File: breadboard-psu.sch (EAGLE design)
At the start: 23 parts, among them J1 DC_IN, J2 5V-BOARD, J3 5V-CABLE, J4 3.3V-BOARD, J5 3.3V-CABLE, K1 POWER, K2 5V, K3 3.3V, U1 AP1117T50G-U, U2 AP1117T33G-U

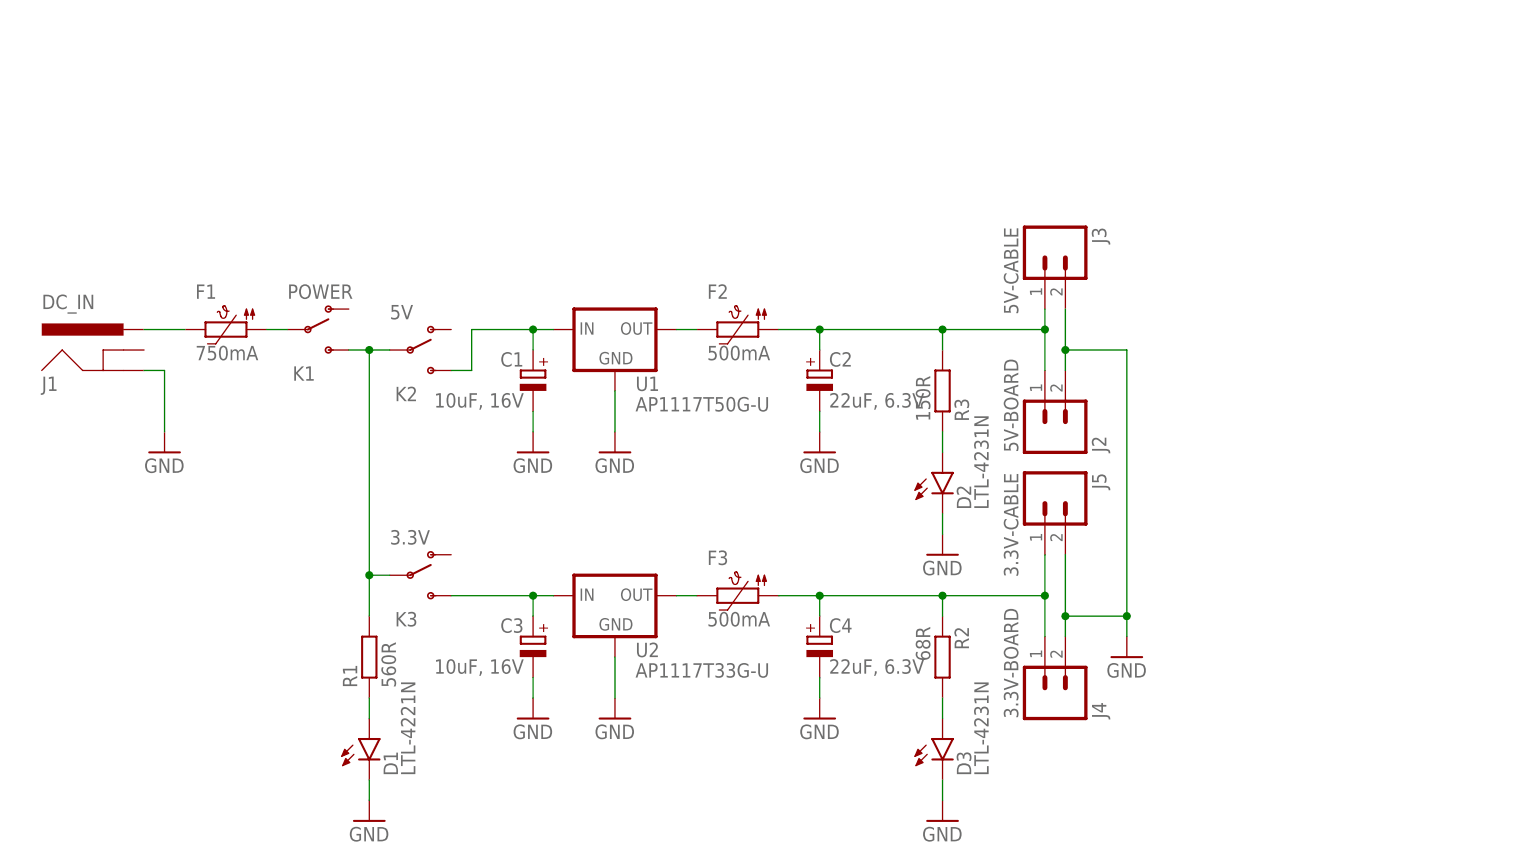
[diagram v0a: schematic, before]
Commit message: UPDATE:  - first draft, schematic is stable, layout is routed and poured.  - still left to do the silkscreen and confirm width (to match breadboard).  - all footprints checked or generated in-situ to match the actual BOM.
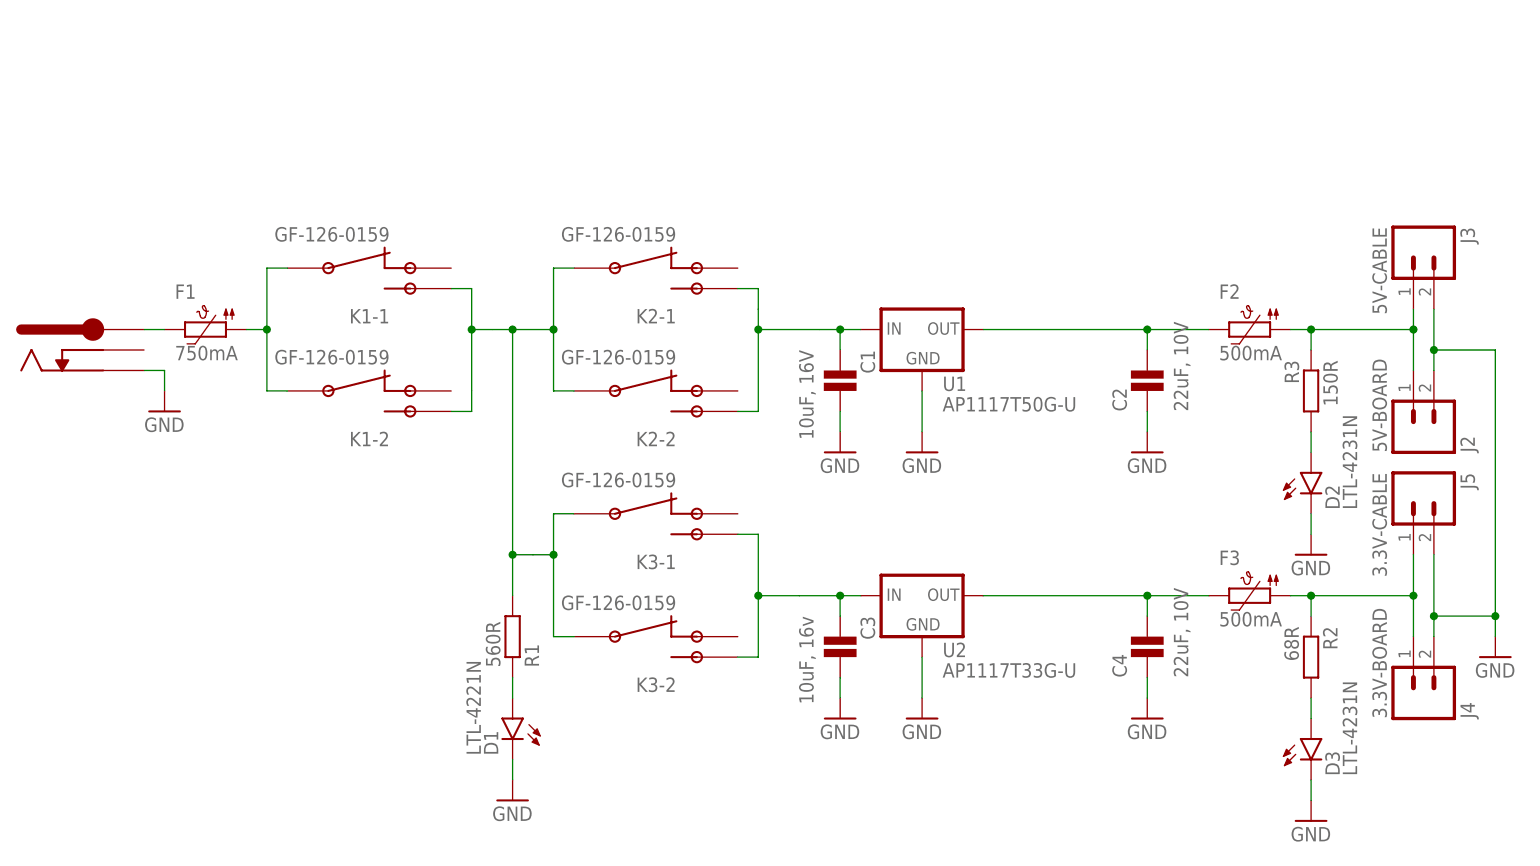
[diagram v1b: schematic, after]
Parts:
- C1: device rcl:CPOL-EUETR3 -> radu-collected:FK26X7R
- C2, C4: value 22uF, 6.3V -> 22uF, 10V; device rcl:CPOL-EUETR3 -> radu-collected:FK20X7R
- C3: value 10uF, 16V -> 10uF, 16v; device rcl:CPOL-EUETR3 -> radu-collected:FK26X7R
- J1: value DC_IN -> 163-5010-E; device SparkFun-Connectors:POWER_JACKSLT -> radu-collected:163-5010-E
- K1: value POWER -> GF-126-0159; device SparkFun-Electromechanical:SWITCH-SPDTPTH -> radu-collected:GF-126-0159
- K2: value 5V -> GF-126-0159; device SparkFun-Electromechanical:SWITCH-SPDTPTH -> radu-collected:GF-126-0159
- K3: value 3.3V -> GF-126-0159; device SparkFun-Electromechanical:SWITCH-SPDTPTH -> radu-collected:GF-126-0159
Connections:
- net 3V3: no longer C4.+
- net 5V: now also R3.1; no longer C2.+, R3.2
- net GND: now also C1.P$2, C2.P$1, C3.P$2, C4.P$1, J1.-; no longer C1.-, C2.-, C3.-, C4.-, J1.GND
- net N$1: now also J1.+; no longer J1.PWR
- net N$10: now also R3.2; no longer R3.1
- net N$2: now also K1-1.P$1, K1-2.P$1; no longer K1.P
- net N$3: now also K1-1.P$3, K1-2.P$3, K2-1.P$1, K2-2.P$1, K3-1.P$1, K3-2.P$1; no longer K1.S, K2.P, K3.P
- net N$4: now also C1.P$1, K2-1.P$3, K2-2.P$3; no longer C1.+, K2.S
- net N$5: now also C3.P$1, K3-1.P$3, K3-2.P$3; no longer C3.+, K3.S
- net N$6: now also C2.P$2
- net N$7: now also C4.P$2
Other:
- moved on the sheet: D1, D2, D3, F1, F2, F3, J2, J3, J4, J5, R1, R2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

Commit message: UPDATE:  - redesigned without fangs as various breadboards have various widths, leaving just cable version in  - this allows us to fit in 5x5cm with drastic reduction in price
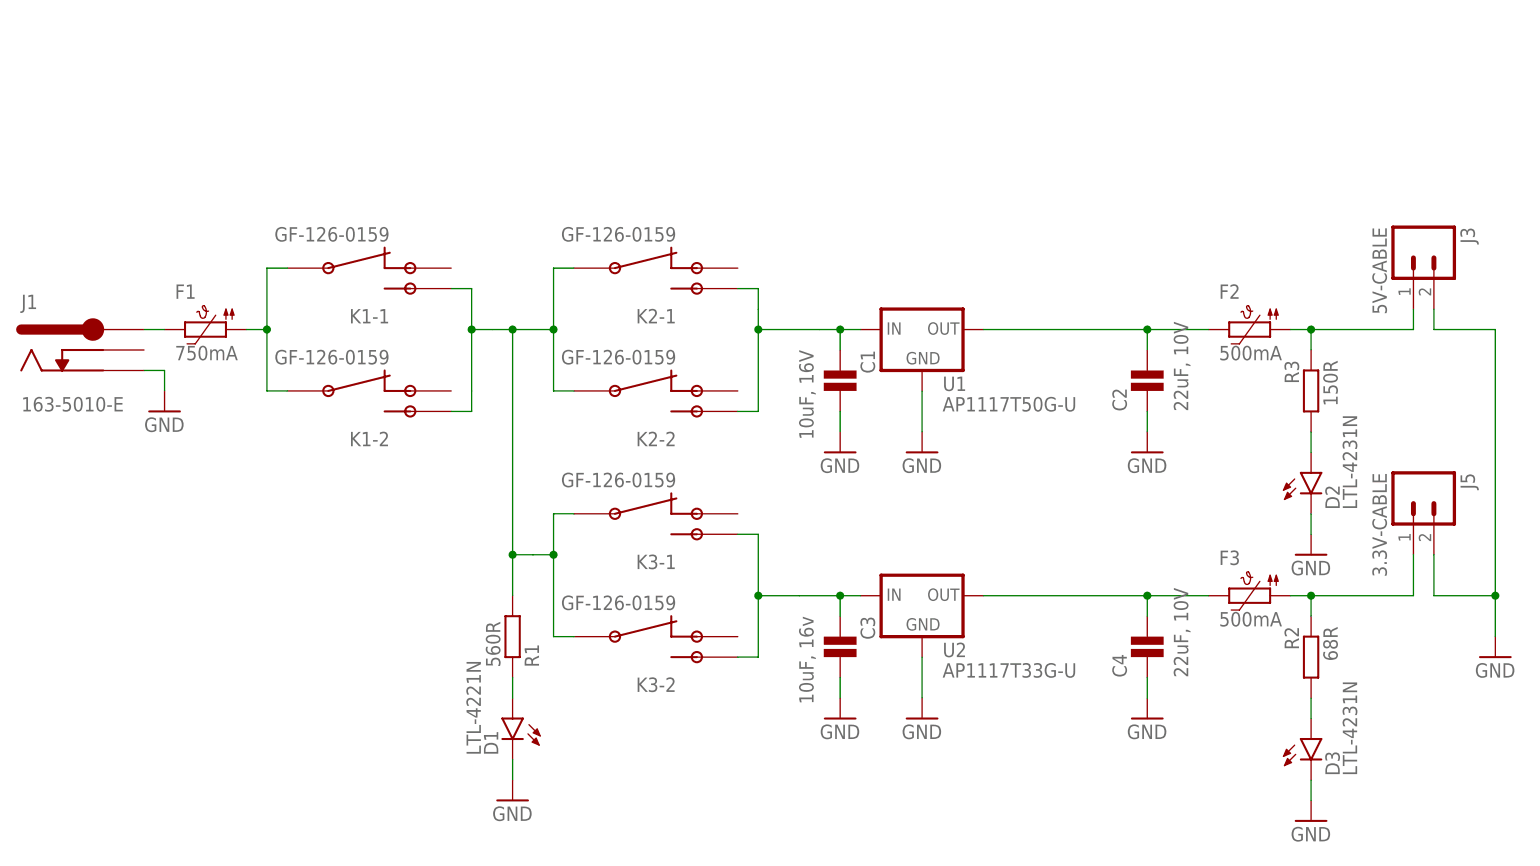
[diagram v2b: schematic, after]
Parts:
- removed J2: 5V-BOARD, SparkFun-Connectors:M02PTH
- removed J4: 3.3V-BOARD, SparkFun-Connectors:M02PTH
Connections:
- net 3V3: no longer J4.1
- net 5V: no longer J2.1
- net GND: no longer J2.2, J4.2
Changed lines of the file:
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@@
 <part name="GND2" library="SparkFun-Aesthetics" deviceset="GND" device=""/>
 <part name="GND3" library="SparkFun-Aesthetics" deviceset="GND" device=""/>
-<part name="J4" library="SparkFun-Connectors" deviceset="M02" device="PTH" value="3.3V-BOARD"/>
-<part name="J2" library="SparkFun-Connectors" deviceset="M02" device="PTH" value="5V-BOARD"/>
 <part name="J3" library="SparkFun-Connectors" deviceset="M02" device="POLAR" value="5V-CABLE"/>
 <part name="J5" library="SparkFun-Connectors" deviceset="M02" device="POLAR" value="3.3V-CABLE"/>
@@
 <instance part="GND2" gate="1" x="154.94" y="96.52"/>
 <instance part="GND3" gate="1" x="154.94" y="63.5"/>
-<instance part="J4" gate="G$1" x="215.9" y="66.04" rot="MR90"/>
-<instance part="J2" gate="G$1" x="215.9" y="99.06" rot="MR90"/>
 <instance part="J3" gate="G$1" x="215.9" y="121.92" rot="R270"/>
 <instance part="J5" gate="G$1" x="215.9" y="91.44" rot="R270"/>
 <instance part="GND5" gate="1" x="226.06" y="71.12"/>
 <instance part="R1" gate="G$1" x="104.14" y="73.66" rot="MR90"/>
-<instance part="R2" gate="G$1" x="203.2" y="71.12" rot="R270"/>
+<instance part="R2" gate="G$1" x="203.2" y="71.12" rot="MR270"/>
 <instance part="R3" gate="G$1" x="203.2" y="104.14" rot="MR270"/>
 <instance part="GND6" gate="1" x="104.14" y="53.34"/>
@@
 <segment>
 <pinref part="J5" gate="G$1" pin="2"/>
-<pinref part="J4" gate="G$1" pin="2"/>
-<wire x1="218.44" y1="83.82" x2="218.44" y2="76.2" width="0.1524" layer="91"/>
+<wire x1="218.44" y1="83.82" x2="218.44" y2="78.74" width="0.1524" layer="91"/>
 <pinref part="GND5" gate="1" pin="GND"/>
-<wire x1="218.44" y1="76.2" x2="218.44" y2="73.66" width="0.1524" layer="91"/>
-<wire x1="218.44" y1="76.2" x2="226.06" y2="76.2" width="0.1524" layer="91"/>
-<wire x1="226.06" y1="76.2" x2="226.06" y2="73.66" width="0.1524" layer="91"/>
-<junction x="218.44" y="76.2"/>
+<wire x1="218.44" y1="78.74" x2="226.06" y2="78.74" width="0.1524" layer="91"/>
+<wire x1="226.06" y1="78.74" x2="226.06" y2="73.66" width="0.1524" layer="91"/>
 <pinref part="J3" gate="G$1" pin="2"/>
-<pinref part="J2" gate="G$1" pin="2"/>
-<wire x1="218.44" y1="114.3" x2="218.44" y2="109.22" width="0.1524" layer="91"/>
-<wire x1="218.44" y1="109.22" x2="218.44" y2="106.68" width="0.1524" layer="91"/>
-<wire x1="218.44" y1="109.22" x2="226.06" y2="109.22" width="0.1524" layer="91"/>
-<junction x="218.44" y="109.22"/>
-<wire x1="226.06" y1="76.2" x2="226.06" y2="109.22" width="0.1524" layer="91"/>
-<junction x="226.06" y="76.2"/>
+<wire x1="218.44" y1="114.3" x2="218.44" y2="111.76" width="0.1524" layer="91"/>
+<wire x1="218.44" y1="111.76" x2="226.06" y2="111.76" width="0.1524" layer="91"/>
+<wire x1="226.06" y1="78.74" x2="226.06" y2="111.76" width="0.1524" layer="91"/>
+<junction x="226.06" y="78.74"/>
 </segment>
 <segment>
@@
 <wire x1="203.2" y1="111.76" x2="215.9" y2="111.76" width="0.1524" layer="91"/>
 <wire x1="215.9" y1="111.76" x2="215.9" y2="114.3" width="0.1524" layer="91"/>
-<pinref part="J2" gate="G$1" pin="1"/>
-<wire x1="215.9" y1="106.68" x2="215.9" y2="111.76" width="0.1524" layer="91"/>
-<junction x="215.9" y="111.76"/>
 <pinref part="R3" gate="G$1" pin="1"/>
 <wire x1="203.2" y1="111.76" x2="203.2" y2="109.22" width="0.1524" layer="91"/>
@@
 <segment>
 <pinref part="J5" gate="G$1" pin="1"/>
-<pinref part="J4" gate="G$1" pin="1"/>
 <wire x1="215.9" y1="83.82" x2="215.9" y2="78.74" width="0.1524" layer="91"/>
-<wire x1="215.9" y1="78.74" x2="215.9" y2="73.66" width="0.1524" layer="91"/>
 <wire x1="203.2" y1="78.74" x2="215.9" y2="78.74" width="0.1524" layer="91"/>
-<junction x="215.9" y="78.74"/>
 <pinref part="R2" gate="G$1" pin="1"/>
 <wire x1="203.2" y1="76.2" x2="203.2" y2="78.74" width="0.1524" layer="91"/>

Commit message: UPDATE:  - PCB done, including silk, aesthetics, physicals and design for manufacturing  - this is ready to go to the fab.
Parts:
- added LOGO2: OSHW-LOGOL, SparkFun-Aesthetics:OSHW-LOGOL
- D1, D2, D3: device SparkFun-LED:LED3MM -> led:LED3MM
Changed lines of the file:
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@@
 <setting verticaltext="up"/>
 </settings>
-<grid distance="0.1" unitdist="inch" unit="inch" style="lines" multiple="1" display="yes" altdistance="0.01" altunitdist="inch" altunit="inch"/>
+<grid distance="0.1" unitdist="inch" unit="inch" style="lines" multiple="1" display="no" altdistance="0.01" altunitdist="inch" altunit="inch"/>
 <layers>
 <layer number="1" name="Top" color="4" fill="1" visible="no" active="no"/>
@@
 <part name="GND7" library="SparkFun-Aesthetics" deviceset="GND" device=""/>
 <part name="GND8" library="SparkFun-Aesthetics" deviceset="GND" device=""/>
-<part name="D1" library="SparkFun-LED" deviceset="LED" device="3MM" value="LTL-4221N"/>
-<part name="D2" library="SparkFun-LED" deviceset="LED" device="3MM" value="LTL-4231N"/>
-<part name="D3" library="SparkFun-LED" deviceset="LED" device="3MM" value="LTL-4231N"/>
 <part name="GND4" library="SparkFun-Aesthetics" deviceset="GND" device=""/>
 <part name="GND9" library="SparkFun-Aesthetics" deviceset="GND" device=""/>
@@
 <part name="C2" library="radu-collected" deviceset="FK20*" device="" technology="X7R" value="22uF, 10V"/>
 <part name="C4" library="radu-collected" deviceset="FK20*" device="" technology="X7R" value="22uF, 10V"/>
+<part name="D1" library="led" deviceset="LED" device="3MM" value="LTL-4221N"/>
+<part name="D3" library="led" deviceset="LED" device="3MM" value="LTL-4231N"/>
+<part name="D2" library="led" deviceset="LED" device="3MM" value="LTL-4231N"/>
+<part name="LOGO2" library="SparkFun-Aesthetics" deviceset="OSHW-LOGO" device="L"/>
 </parts>
 <sheets>
@@
 <instance part="GND7" gate="1" x="203.2" y="50.8"/>
 <instance part="GND8" gate="1" x="203.2" y="83.82"/>
-<instance part="D1" gate="G$1" x="104.14" y="63.5" rot="MR0"/>
-<instance part="D2" gate="G$1" x="203.2" y="93.98"/>
-<instance part="D3" gate="G$1" x="203.2" y="60.96"/>
 <instance part="GND4" gate="1" x="144.78" y="96.52"/>
 <instance part="GND9" gate="1" x="182.88" y="96.52"/>
@@
 <instance part="C2" gate="G$1" x="182.88" y="104.14" rot="R90"/>
 <instance part="C4" gate="G$1" x="182.88" y="71.12" rot="R90"/>
+<instance part="D1" gate="G$1" x="104.14" y="63.5"/>
+<instance part="D3" gate="G$1" x="203.2" y="60.96"/>
+<instance part="D2" gate="G$1" x="203.2" y="93.98"/>
+<instance part="LOGO2" gate="G$1" x="76.2" y="144.78"/>
 </instances>
 <busses>
@@
 </segment>
 <segment>
-<pinref part="D1" gate="G$1" pin="C"/>
 <pinref part="GND6" gate="1" pin="GND"/>
 <wire x1="104.14" y1="58.42" x2="104.14" y2="55.88" width="0.1524" layer="91"/>
-</segment>
-<segment>
-<pinref part="D2" gate="G$1" pin="C"/>
+<pinref part="D1" gate="G$1" pin="C"/>
+</segment>
+<segment>
 <pinref part="GND8" gate="1" pin="GND"/>
 <wire x1="203.2" y1="88.9" x2="203.2" y2="86.36" width="0.1524" layer="91"/>
-</segment>
-<segment>
-<pinref part="D3" gate="G$1" pin="C"/>
+<pinref part="D2" gate="G$1" pin="C"/>
+</segment>
+<segment>
 <pinref part="GND7" gate="1" pin="GND"/>
 <wire x1="203.2" y1="55.88" x2="203.2" y2="53.34" width="0.1524" layer="91"/>
+<pinref part="D3" gate="G$1" pin="C"/>
 </segment>
 <segment>
@@
 <segment>
 <pinref part="R1" gate="G$1" pin="1"/>
+<wire x1="104.14" y1="68.58" x2="104.14" y2="66.04" width="0.1524" layer="91"/>
 <pinref part="D1" gate="G$1" pin="A"/>
-<wire x1="104.14" y1="68.58" x2="104.14" y2="66.04" width="0.1524" layer="91"/>
 </segment>
 </net>
 <net name="N$10" class="0">
 <segment>
-<pinref part="D2" gate="G$1" pin="A"/>
 <pinref part="R3" gate="G$1" pin="2"/>
 <wire x1="203.2" y1="96.52" x2="203.2" y2="99.06" width="0.1524" layer="91"/>
+<pinref part="D2" gate="G$1" pin="A"/>
 </segment>
 </net>
@@
 <segment>
 <pinref part="R2" gate="G$1" pin="2"/>
+<wire x1="203.2" y1="66.04" x2="203.2" y2="63.5" width="0.1524" layer="91"/>
 <pinref part="D3" gate="G$1" pin="A"/>
-<wire x1="203.2" y1="66.04" x2="203.2" y2="63.5" width="0.1524" layer="91"/>
-</segment>
-</net>
+</segment>
+</net>
